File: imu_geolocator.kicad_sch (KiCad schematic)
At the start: 35 parts, among them J1 Conn_01x05_Pin, J2 Conn_01x08_Pin, Q1 PMOS, U1 STM32WLE5C8Ux, U2 TPS62202DBV, U3 ICM-42688-P, U4 AK09918C

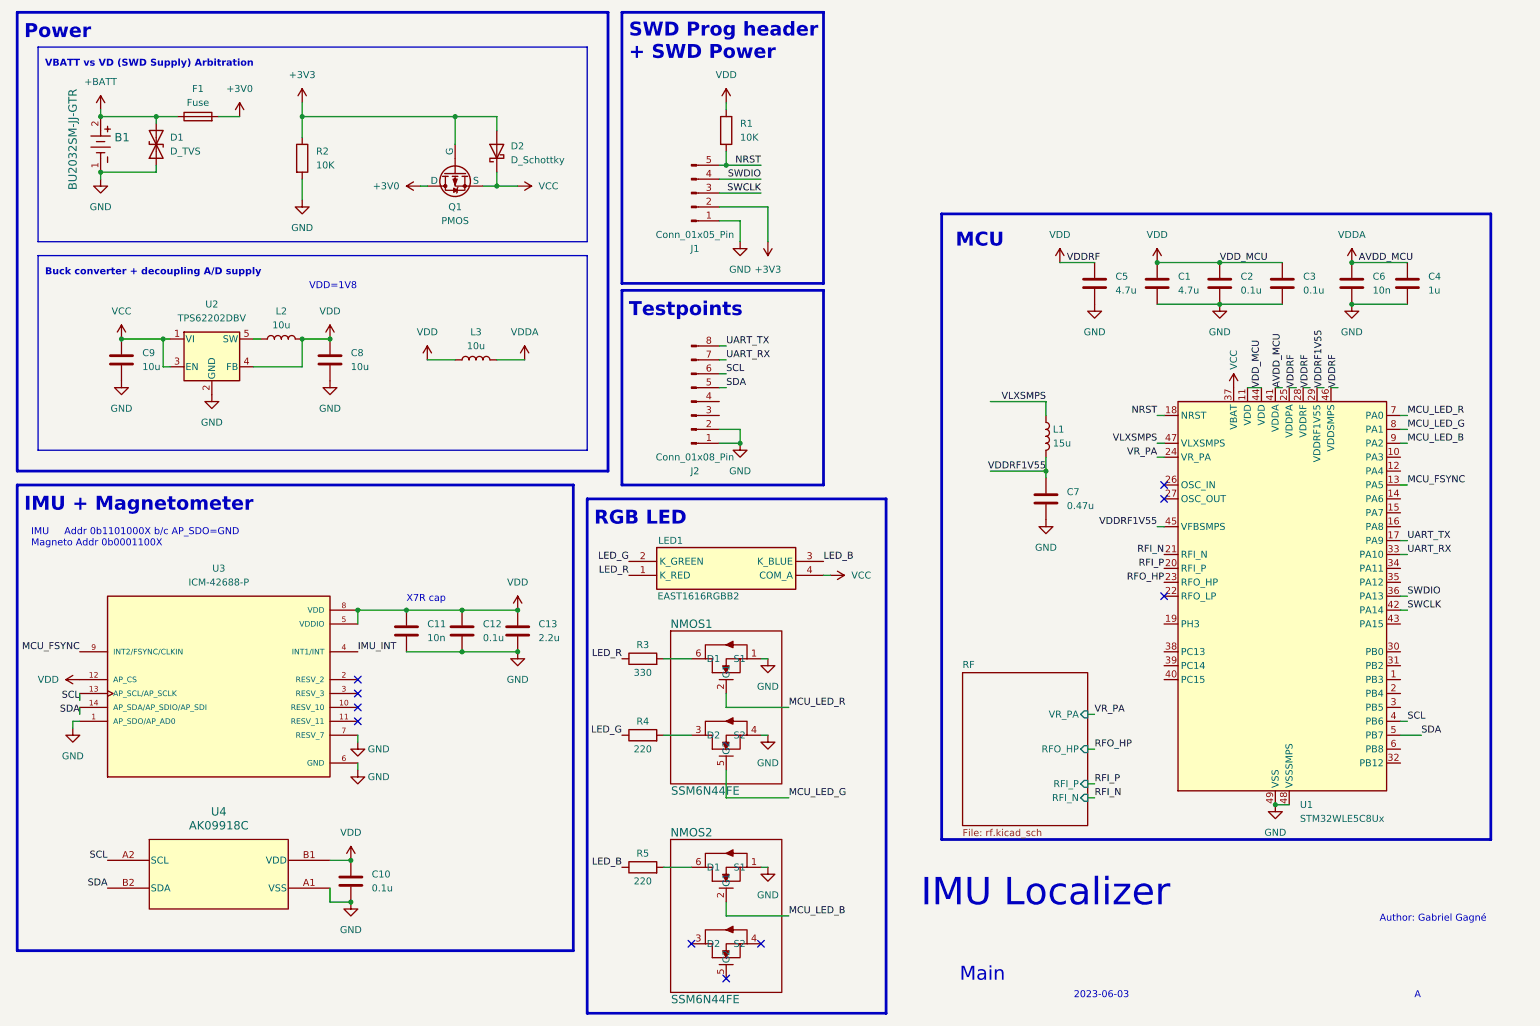
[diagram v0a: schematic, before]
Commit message: Finished schematic v1, start PCB
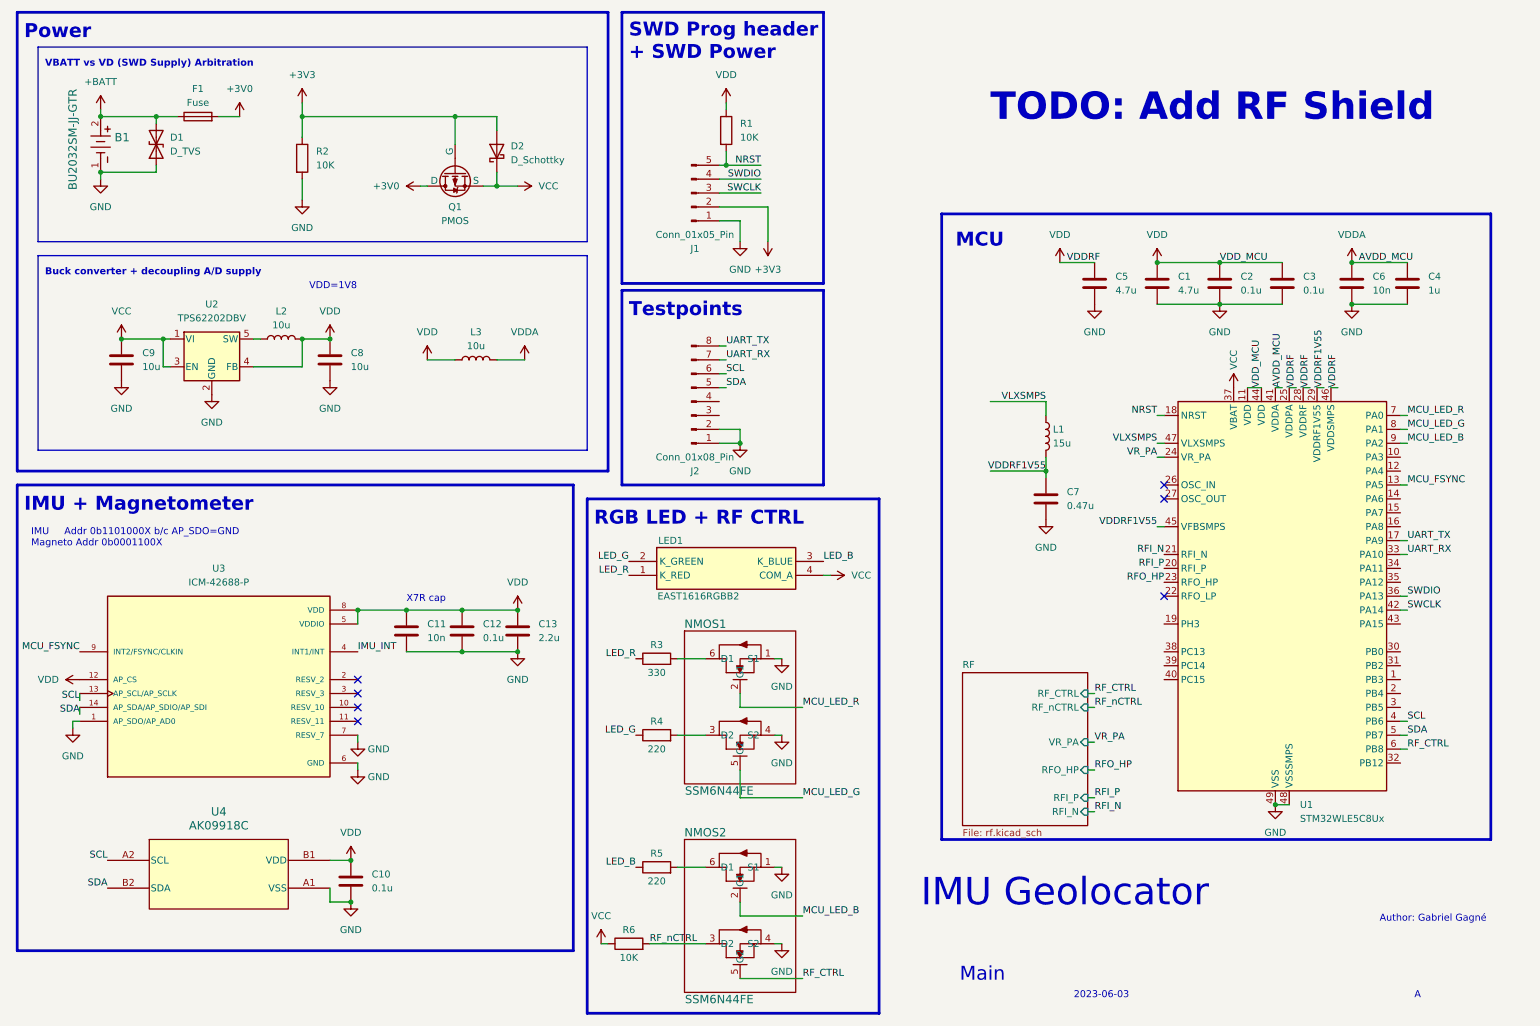
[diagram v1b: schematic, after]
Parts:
- added R6: 10K, Resistor_SMD:R_0603_1608Metric, symbol Device:R
- B1: footprint BU2032SM-JJ-GTR_MPD -> BU2032SM-JJ-GTR:BU2032SM-JJ-GTR_MPD
- C1, C10, C11, C12, C13, C2, C3, C4, C5, C6, C7, C8, C9: footprint (none) -> Capacitor_SMD:C_0603_1608Metric
- J1: footprint (none) -> Connector_PinHeader_2.54mm:PinHeader_1x05_P2.54mm_Vertical
- J2: footprint (none) -> Connector_PinHeader_2.54mm:PinHeader_1x08_P2.54mm_Vertical
- L1, L2, L3: footprint (none) -> Inductor_SMD:L_0603_1608Metric
- LED1: footprint EAST1616RGBB2 -> EAST1616RGBB2:EAST1616RGBB2
- NMOS1, NMOS2: footprint ES6 -> SSM6N44FE,LM:ES6
- R1, R2, R3, R4, R5: footprint (none) -> Resistor_SMD:R_0603_1608Metric
- U3: footprint PQFN50P300X250X97-14N -> ICM-42688-P:PQFN50P300X250X97-14N
- U4: footprint BGA4_WL-CSP_AKM -> AK09918C:BGA4_WL-CSP_AKM
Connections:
- net GND: now also NMOS2.4 (S2)
- net VCC: now also R6.1
- net RF_nCTRL: now reaches NMOS2.3 (D2)
- net RF_nCTRL: now also R6.2
- net RF_CTRL: now reaches NMOS2.5 (G2)
- net RF_CTRL: now also U1.6 (PB8)
- no-connect marks 10 -> 7
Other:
- sheet RF ports: added RF_CTRL, RF_nCTRL; removed none
- note added: "IMU Geolocator"
- note added: "RGB LED + RF CTRL"
- note added: "TODO: Add RF Shield"
- note removed: "IMU Localizer"
- note removed: "RGB LED"
- moved on the sheet: NMOS1, NMOS2, R3, R4, R5

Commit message: Routing in progress
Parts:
- removed L3: 10u, Inductor_SMD:L_0603_1608Metric, symbol Device:L
- added FB1: FerriteBead, Inductor_SMD:L_0603_1608Metric, symbol Device:FerriteBead
- added R7, R8: 10K, Resistor_SMD:R_0603_1608Metric, symbol Device:R
- L1: footprint Inductor_SMD:L_0603_1608Metric -> Inductor_SMD:L_0805_2012Metric; Link (none) -> https://www.digikey.ca/en/products/detail/tdk-corporation/M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
- L2: footprint Inductor_SMD:L_0603_1608Metric -> Inductor_SMD:L_0805_2012Metric
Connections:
- net IMU_INT: now also U1.13 (PA5)
- net MCU_FSYNC: now also U1.12 (PA4); no longer U1.13 (PA5)
- net SCL: now also R7.1
- net SDA: now also R8.1
- net VCC: no longer R6.1, U1.37 (VBAT)
- net VDD: now also R6.1, U1.37 (VBAT), FB1.1, R7.2, R8.2
- net VDDA: now also FB1.2

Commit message: Schematic done
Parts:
- removed C13: 2.2u, Capacitor_SMD:C_0603_1608Metric, symbol Device:C
- removed C5: 4.7u, Capacitor_SMD:C_0603_1608Metric, symbol Device:C
- removed C7: 0.47u, Capacitor_SMD:C_0603_1608Metric, symbol Device:C
- removed L1: 15u, Inductor_SMD:L_0805_2012Metric, symbol Device:L
- removed R6: 10K, Resistor_SMD:R_0603_1608Metric, symbol Device:R
- removed U1: STM32WLE5C8Ux, Package_DFN_QFN:QFN-48-1EP_7x7mm_P0.5mm_EP5.6x5.6mm, symbol MCU_ST_STM32WL:STM32WLE5C8Ux
- added C6: 1u, Capacitor_SMD:C_0603_1608Metric, symbol Device:C
- added U4: STM32L431CCTx, Package_QFP:LQFP-48_7x7mm_P0.5mm, symbol MCU_ST_STM32L4:STM32L431CCTx
- B1: Link (none) -> https://www.digikey.ca/en/products/detail/mpd-memory-protec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
- C1: renamed from C9; Link (none) -> https://www.digikey.ca/en/products/detail/samsung-electro-m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
- C10: renamed from C6; Link (none) -> https://www.digikey.ca/en/products/detail/kemet/C0603X103J4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
- C11: renamed from C4; Link (none) -> https://www.digikey.ca/en/products/detail/samsung-electro-m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
- C2: renamed from C8; Link (none) -> https://www.digikey.ca/en/products/detail/samsung-electro-m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
- C3: renamed from C10; Link (none) -> https://www.digikey.ca/en/products/detail/samsung-electro-m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
- C4: renamed from C11; Link (none) -> https://www.digikey.ca/en/products/detail/kemet/C0603X103J4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
- C5: renamed from C12; Link (none) -> https://www.digikey.ca/en/products/detail/samsung-electro-m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
- C7: renamed from C1; Link (none) -> https://www.digikey.ca/en/products/detail/samsung-electro-m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
- C8: renamed from C2; Link (none) -> https://www.digikey.ca/en/products/detail/samsung-electro-m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
- C9: renamed from C3; Link (none) -> https://www.digikey.ca/en/products/detail/samsung-electro-m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
- L1: renamed from L2; footprint Inductor_SMD:L_0805_2012Metric -> Inductor_SMD:L_Changjiang_FNR6028S; Link (none) -> https://www.digikey.ca/en/products/detail/taiyo-yuden/NR602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
- LED1: Height 0.45 -> (none); Manufacturer_Name Everlight -> (none); Manufacturer_Part_Number EAST1616RGBB2 -> (none)
- NMOS1, NMOS2: Link (none) -> https://www.digikey.ca/en/products/detail/toshiba-semicondu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
- R1: renamed from R2; Link (none) -> https://www.digikey.ca/en/products/detail/yageo/RC0603FR-07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
- R2: renamed from R7; Link (none) -> https://www.digikey.ca/en/products/detail/yageo/RC0603FR-07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
- R3: renamed from R8; Link (none) -> https://www.digikey.ca/en/products/detail/yageo/RC0603FR-07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
- R4: renamed from R3; Link (none) -> https://www.digikey.ca/en/products/detail/yageo/RC0603JR-07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
- R5: renamed from R4; Link (none) -> https://www.digikey.ca/en/products/detail/walsin-technology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
- R6: renamed from R5; Link (none) -> https://www.digikey.ca/en/products/detail/walsin-technology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
- R7: renamed from R1; Link (none) -> https://www.digikey.ca/en/products/detail/yageo/RC0603FR-07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
- U3: MANUFACTURER TDK InvenSense -> (none); MAXIMUM_PACKAGE_HEIGHT 0.97mm -> (none); PARTREV 1.2 -> (none); STANDARD IPC-7351B -> (none)
- renumbered U4 to U1
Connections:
- net GND: now also C6.2, U4.23 (VSS), U4.35 (VSS), U4.47 (VSS), U4.8 (VSSA); no longer NMOS2.4 (S2)
- net IMU_INT: now also U4.19 (PB1)
- net MCU_FSYNC: now also U4.20 (PB2)
- net MCU_LED_B: now also U4.12 (PA2)
- net MCU_LED_G: now also U4.11 (PA1)
- net MCU_LED_R: now also U4.10 (PA0)
- net NRST: now also U4.7 (NRST)
- net SCL: now also U4.30 (PA9)
- net SDA: now also U4.31 (PA10)
- net SWCLK: now also U4.37 (PA14)
- net SWDIO: now also U4.34 (PA13)
- net UART_RX: now also U4.42 (PB6)
- net UART_TX: now also U4.43 (PB7)
- net VCC: now also J2.3 (Pin_3)
- net VDD: now also J2.4 (Pin_4), C6.1, U4.1 (VBAT), U4.24 (VDD), U4.36 (VDD), U4.48 (VDD)
- net VDDA: now also U4.9 (VDDA)
- net RF_CTRL: no longer names the net of NMOS2.5 (G2)
- net RF_nCTRL: no longer names the net of NMOS2.3 (D2)
- no-connect marks 7 -> 10
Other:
- removed sheet RF
- note added: "2023-06-04"
- note added: "L431-A"
- note added: "RGB LED"
- note removed: "2023-06-03"
- note removed: "A"
- note removed: "RGB LED + RF CTRL"
- note removed: "TODO: Add RF Shield"
- note removed: "X7R cap"
- moved on the sheet: C10, C11, C7, C8, C9

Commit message: version 0.1-loraless finished
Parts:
- D1: Link (none) -> https://www.digikey.ca/en/products/detail/diodes-incorporat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
- L1: Link https://www.digikey.ca/en/products/detail/taiyo-yuden/NR602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 -> https://www.digikey.ca/en/products/detail/taiyo-yuden/NRS60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
- U4: Link https://www.digikey.ca/en/products/detail/stmicroelectronics/STM32L431CCT6TR/8257907 -> https://www.digikey.ca/en/products/detail/stmicroelectronics/STM32L431CCT6/6621814
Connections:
- net UART_RX: now also J2.8 (Pin_8), U4.43 (PB7); no longer J2.7 (Pin_7), U4.42 (PB6)
- net UART_TX: now also J2.7 (Pin_7), U4.42 (PB6); no longer J2.8 (Pin_8), U4.43 (PB7)
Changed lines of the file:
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@@
   (junction (at 29.21 33.02) (diameter 0) (color 0 0 0 0)
   )
-  (junction (at 66.04 73.66) (diameter 0) (color 0 0 0 0)
-  )
   (junction (at 101.6 45.72) (diameter 0) (color 0 0 0 0)
+  )
+  (junction (at 67.31 73.66) (diameter 0) (color 0 0 0 0)
   )
   (junction (at 66.04 33.02) (diameter 0) (color 0 0 0 0)
@@
     (stroke (width 0) (type default))
   )
+  (wire (pts (xy 67.31 73.66) (xy 71.12 73.66))
+    (stroke (width 0) (type default))
+  )
   (wire (pts (xy 71.12 173.99) (xy 71.12 176.53))
     (stroke (width 0) (type default))
   )
-  (wire (pts (xy 66.04 73.66) (xy 71.12 73.66))
-    (stroke (width 0) (type default))
-  )
   (wire (pts (xy 142.24 77.47) (xy 143.51 77.47))
     (stroke (width 0) (type default))
@@
     (stroke (width 0) (type default))
   )
-  (wire (pts (xy 57.15 78.74) (xy 66.04 78.74))
+  (wire (pts (xy 57.15 78.74) (xy 67.31 78.74))
     (stroke (width 0) (type default))
   )
@@
     (stroke (width 0) (type default))
   )
+  (wire (pts (xy 233.68 157.48) (xy 233.68 156.21))
+    (stroke (width 0) (type default))
+  )
   (wire (pts (xy 142.24 85.09) (xy 156.21 85.09))
     (stroke (width 0) (type default))
@@
     (stroke (width 0) (type default))
   )
-  (wire (pts (xy 66.04 78.74) (xy 66.04 73.66))
+  (wire (pts (xy 67.31 78.74) (xy 67.31 73.66))
     (stroke (width 0) (type default))
   )
@@
   )
   (wire (pts (xy 41.91 78.74) (xy 40.64 78.74))
+    (stroke (width 0) (type default))
+  )
+  (wire (pts (xy 67.31 73.66) (xy 66.04 73.66))
     (stroke (width 0) (type default))
   )
@@
     (fill (type none))
   )
-  (rectangle (start 124.46 64.77) (end 161.29 100.33)
+  (rectangle (start 124.46 64.77) (end 165.1 100.33)
     (stroke (width 0.5) (type default))
     (fill (type none))
@@
     (effects (font (size 1.27 1.27)) (justify right bottom))
   )
-  (label "UART_TX" (at 143.51 74.93 0) (fields_autoplaced)
+  (label "UART_RX" (at 143.51 74.93 0) (fields_autoplaced)
     (effects (font (size 1.27 1.27)) (justify left bottom))
   )
@@
     (effects (font (size 1.27 1.27)) (justify right bottom))
   )
-  (label "UART_RX" (at 217.17 125.73 180) (fields_autoplaced)
+  (label "UART_TX" (at 217.17 125.73 180) (fields_autoplaced)
     (effects (font (size 1.27 1.27)) (justify right bottom))
   )
@@
     (effects (font (size 1.27 1.27)) (justify right bottom))
   )
-  (label "UART_TX" (at 217.17 128.27 180) (fields_autoplaced)
+  (label "UART_RX" (at 217.17 128.27 180) (fields_autoplaced)
     (effects (font (size 1.27 1.27)) (justify right bottom))
   )
@@
     (effects (font (size 1.27 1.27)) (justify right bottom))
   )
-  (label "UART_RX" (at 143.51 77.47 0) (fields_autoplaced)
+  (label "UART_TX" (at 143.51 77.47 0) (fields_autoplaced)
     (effects (font (size 1.27 1.27)) (justify left bottom))
   )
@@
       (effects (font (size 1.27 1.27)) hide)
     )
-    (property "Link" "https://www.digikey.ca/en/products/detail/stmicroelectronics/STM32L431CCT6TR/8257907" (at 233.68 118.11 0)
+    (property "Link" "https://www.digikey.ca/en/products/detail/stmicroelectronics/STM32L431CCT6/6621814" (at 233.68 118.11 0)
       (effects (font (size 1.27 1.27)) hide)
     )
@@
       (effects (font (size 1.27 1.27)) hide)
     )
+    (property "Link" "https://www.digikey.ca/en/products/detail/diodes-incorporated/D5V0L1B2WS-7/2918767" (at 39.37 38.1 90)
+      (effects (font (size 1.27 1.27)) hide)
+    )
     (pin "1")
     (pin "2")
@@
     )
   )
-  (symbol (lib_id "power:GND") (at 233.68 156.21 0) (unit 1)
-    (in_bom yes) (on_board yes) (dnp no) (fields_autoplaced)
-    (property "Reference" "#PWR038" (at 233.68 162.56 0)
-      (effects (font (size 1.27 1.27)) hide)
-    )
-    (property "Value" "GND" (at 233.68 161.29 0)
-      (effects (font (size 1.27 1.27)))
-    )
-    (property "Footprint" "" (at 233.68 156.21 0)
-      (effects (font (size 1.27 1.27)) hide)
-    )
-    (property "Datasheet" "" (at 233.68 156.21 0)
+  (symbol (lib_id "power:GND") (at 233.68 157.48 0) (unit 1)
+    (in_bom yes) (on_board yes) (dnp no) (fields_autoplaced)
+    (property "Reference" "#PWR038" (at 233.68 163.83 0)
+      (effects (font (size 1.27 1.27)) hide)
+    )
+    (property "Value" "GND" (at 233.68 162.56 0)
+      (effects (font (size 1.27 1.27)))
+    )
+    (property "Footprint" "" (at 233.68 157.48 0)
+      (effects (font (size 1.27 1.27)) hide)
+    )
+    (property "Datasheet" "" (at 233.68 157.48 0)
       (effects (font (size 1.27 1.27)) hide)
     )
@@
       (effects (font (size 1.27 1.27)) hide)
     )
-    (property "Link" "https://www.digikey.ca/en/products/detail/taiyo-yuden/NR6028T100M/1866185" (at 62.23 73.66 90)
-      (effects (font (size 1.27 1.27)) hide)
-    )
+    (property "Link" "https://www.digikey.ca/en/products/detail/taiyo-yuden/NRS6045T100MMGK/2665984" (at 62.23 73.66 90)
+      (effects (font (size 1.27 1.27)) hide)
+    )
